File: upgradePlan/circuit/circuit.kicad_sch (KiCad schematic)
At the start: 24 parts, among them J1 Connector_GY_521, M1 Motor_DC, M2 Motor_Servo, Q1 BD249, Q2 BD249, SW1 SW_DIP_x01, U1 Freenove-SP32-WROVER, U2 L293D, U3 LM317_TO-220, U5 LM317_TO-220

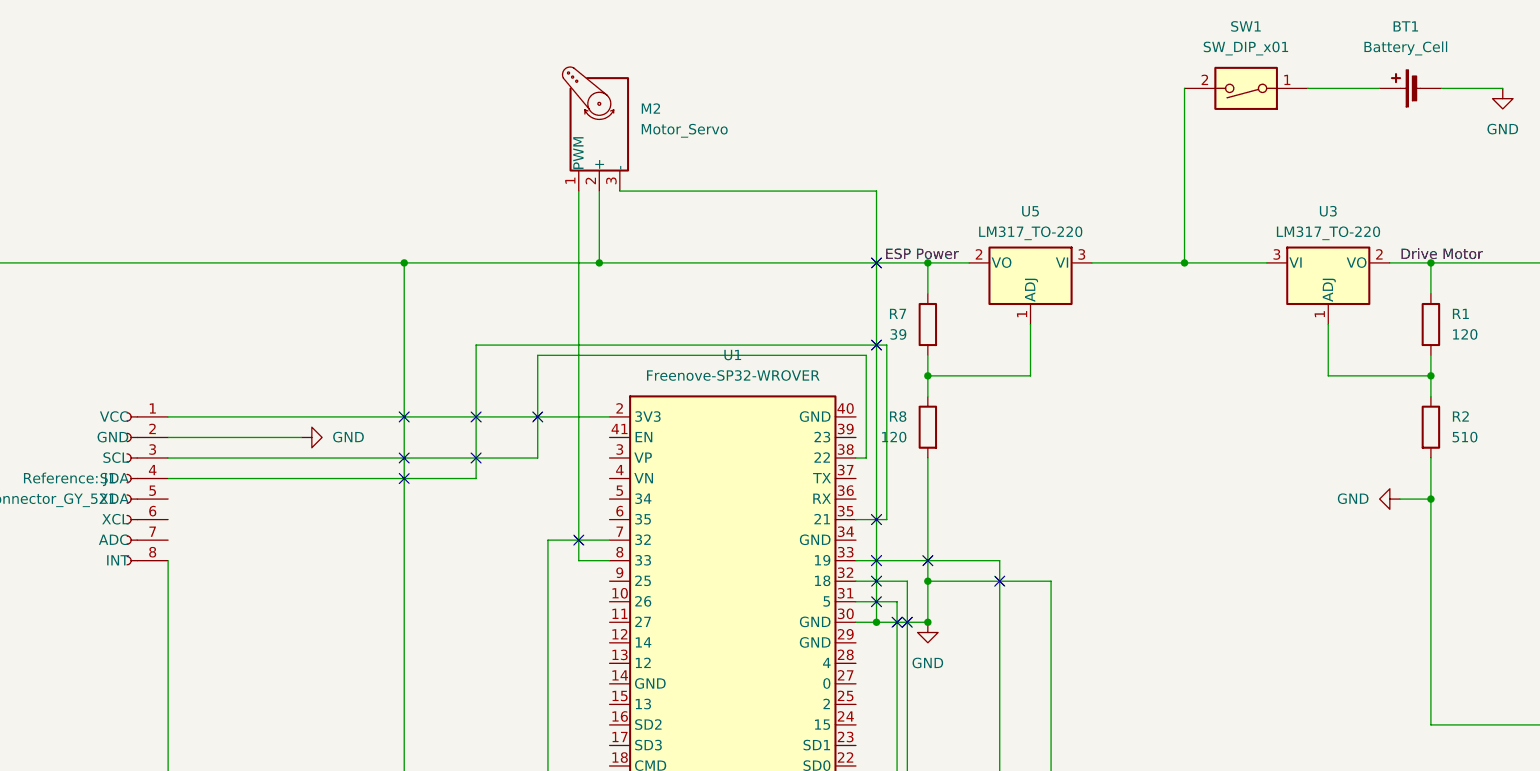
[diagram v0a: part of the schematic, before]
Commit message: Added the HC_SR04 and the tof sensor to the schematic added the recommended changes Update the read me add datasheet for hc-sr04
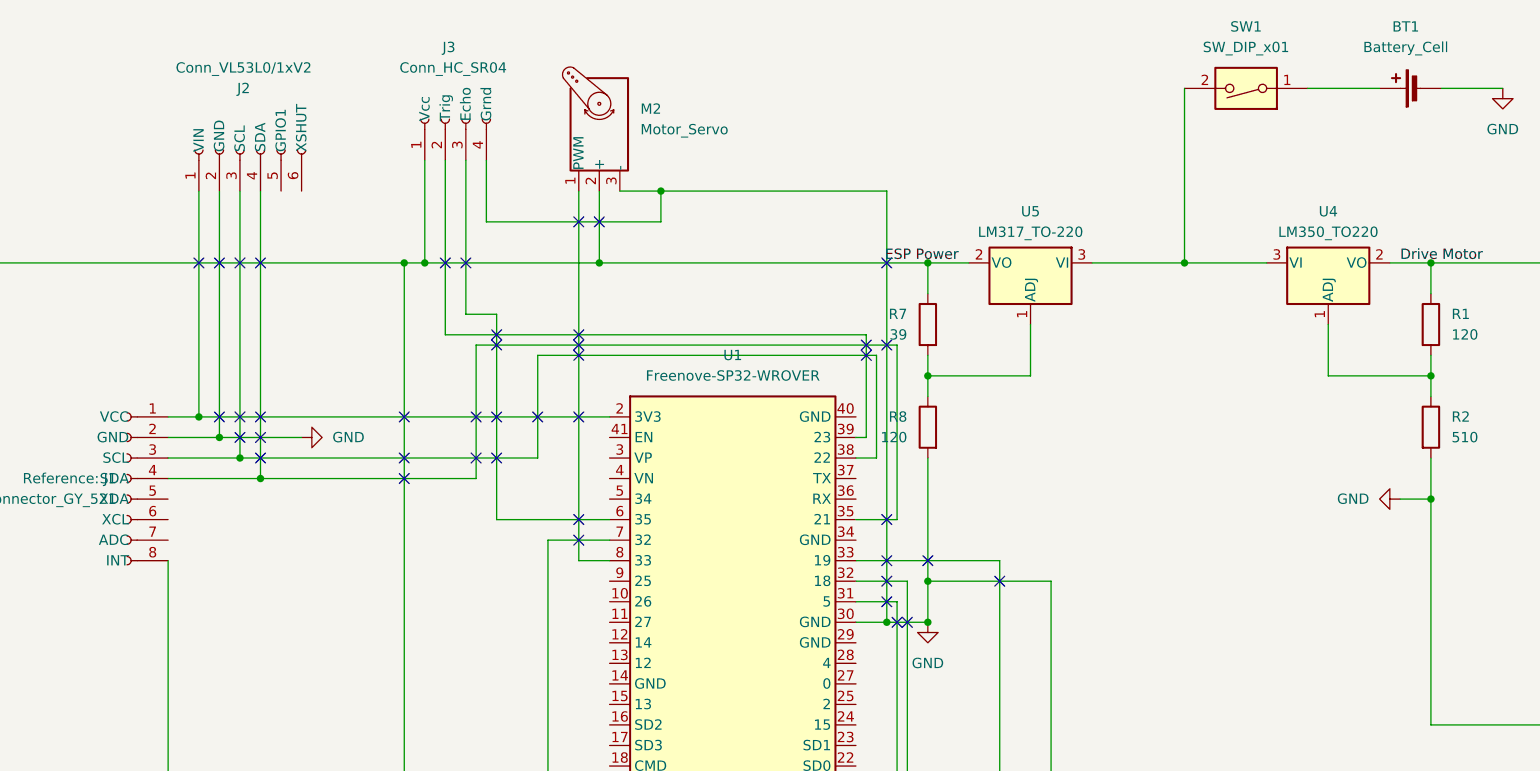
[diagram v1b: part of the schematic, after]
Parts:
- removed U3: LM317_TO-220, Package_TO_SOT_THT:TO-220-3_Vertical, symbol Regulator_Linear:LM317_TO-220
- added J2: Conn_VL53L0/1xV2, symbol Connector:Conn_01x06_Socket
- added J3: Conn_HC_SR04, symbol Connector:Conn_01x04_Socket
- added U4: LM350_TO220, Package_TO_SOT_THT:TO-220-3_Vertical, symbol Regulator_Linear:LM350_TO220
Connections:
- net Drive Motor: now also U4.2 (VO)
- net ESP Power: now also J3.1 (Vcc)
- net GND: now also J2.2 (GND), J3.4 (Grnd)
- net at SW1.2, U5.3 (VI): now also U4.3 (VI)
- net at R1.2, R2.1: now also U4.1 (ADJ)
- net at J1.1 (VCC), U1.2 (3V3): now also J2.1 (VIN)
- net at J1.3 (SCL), U1.38 (22): now also J2.3 (SCL)
- net at J1.4 (SDA), U1.35 (21): now also J2.4 (SDA)
- net at U1.39 (23): now also J3.2 (Trig)
- net at U1.6 (35): now also J3.3 (Echo)
- no-connect marks 30 -> 55

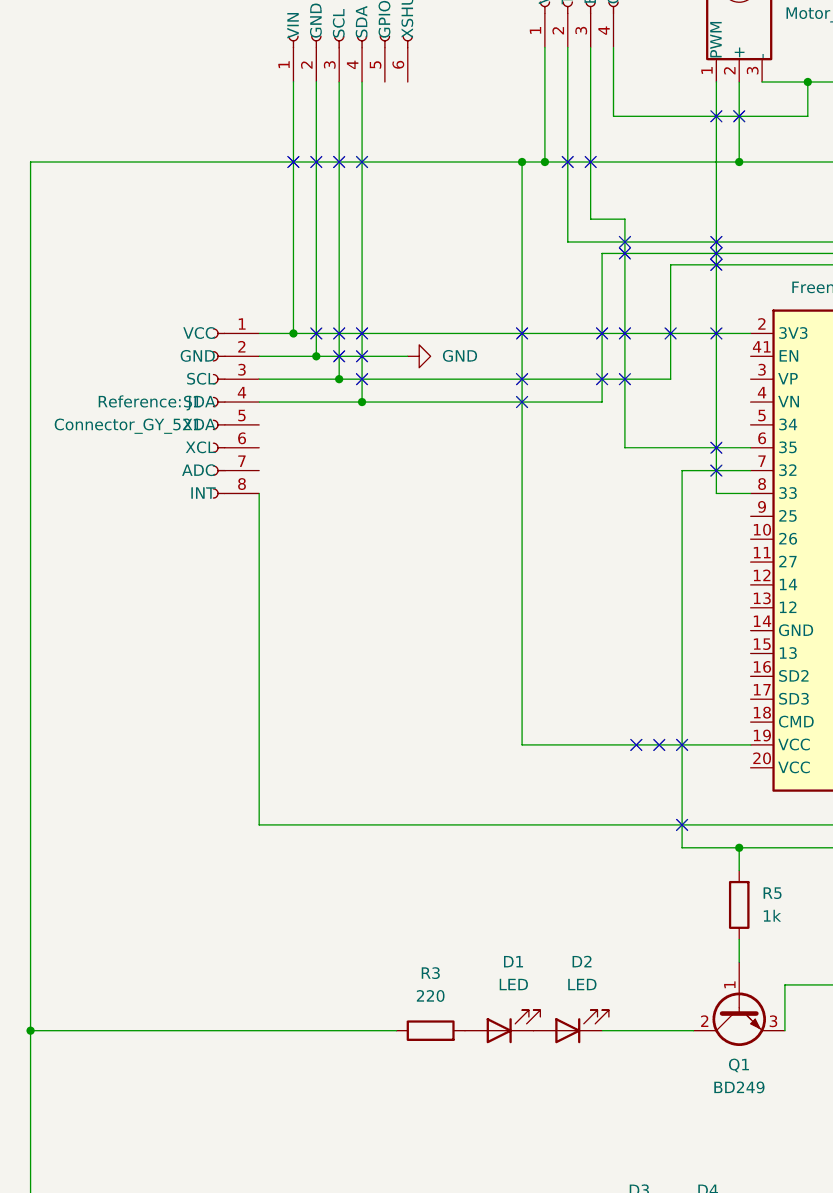
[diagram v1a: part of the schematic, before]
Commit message: Added resistor to I2C bus added setup and reading for ultrasound and tof sensor increased the max number of pub ERROR in Timer creation of the UltraSoundSensor when all others are initilized
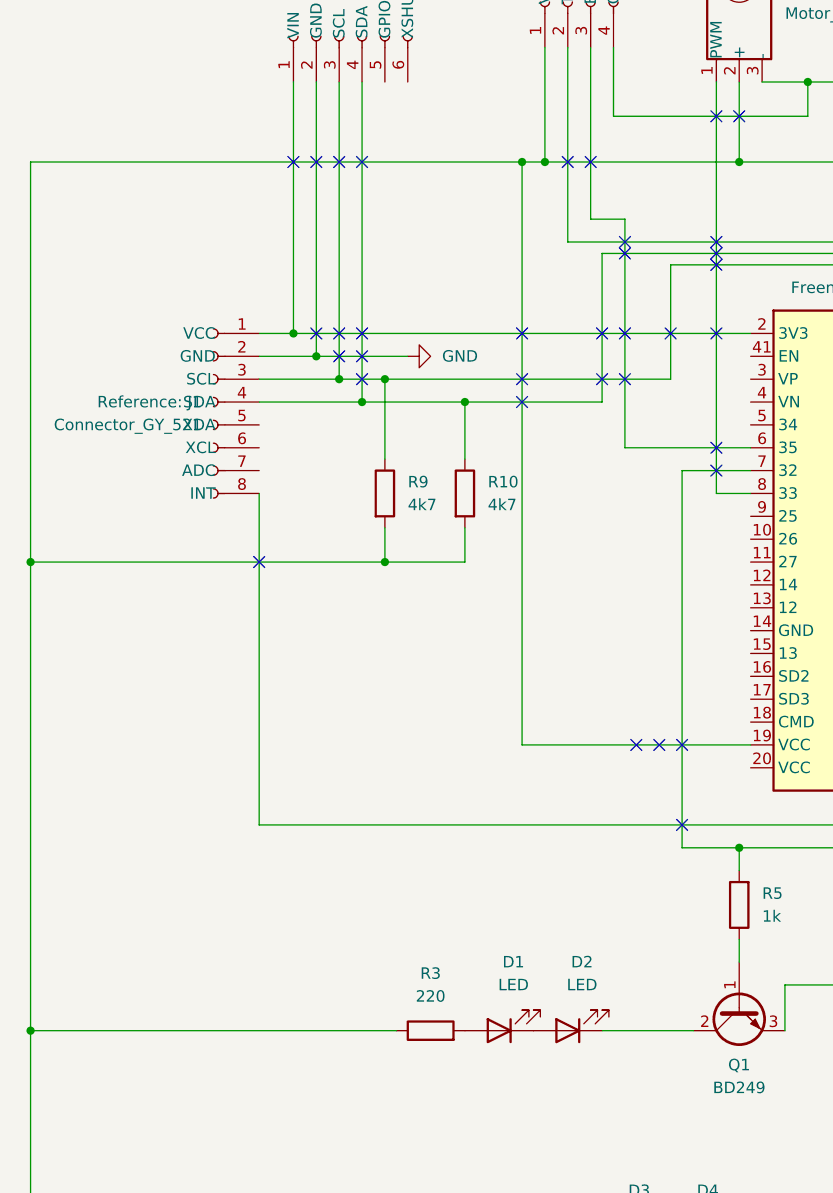
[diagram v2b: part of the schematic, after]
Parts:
- added R10, R9: 4k7, symbol Device:R
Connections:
- net ESP Power: now also R10.2, R9.2
- net at J1.3 (SCL), J2.3 (SCL), U1.38 (22): now also R9.1
- net at J1.4 (SDA), J2.4 (SDA), U1.35 (21): now also R10.1
- no-connect marks 55 -> 56
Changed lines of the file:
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@@
   (junction (at 200.66 76.2) (diameter 0) (color 0 0 0 0)
   )
+  (junction (at 67.31 73.66) (diameter 0) (color 0 0 0 0)
+  )
   (junction (at 138.43 46.99) (diameter 0) (color 0 0 0 0)
   )
@@
   (junction (at 153.67 138.43) (diameter 0) (color 0 0 0 0)
   )
+  (junction (at 58.42 91.44) (diameter 0) (color 0 0 0 0)
+  )
+  (junction (at 19.05 91.44) (diameter 0) (color 0 0 0 0)
+  )
   (junction (at 97.79 123.19) (diameter 0) (color 0 0 0 0)
   )
@@
   )
   (junction (at 48.26 66.04) (diameter 0) (color 0 0 0 0)
+  )
+  (junction (at 58.42 71.12) (diameter 0) (color 0 0 0 0)
   )
   (junction (at 266.7 72.39) (diameter 0) (color 0 0 0 0)
@@
   (no_connect (at 133.35 46.99))
   (no_connect (at 90.17 66.04))
+  (no_connect (at 44.45 91.44))
   (no_connect (at 91.44 111.76))
   (no_connect (at 53.34 68.58))
@@
     (stroke (width 0) (type default))
   )
+  (wire (pts (xy 67.31 87.63) (xy 67.31 91.44))
+    (stroke (width 0) (type default))
+  )
   (wire (pts (xy 97.79 38.1) (xy 97.79 46.99))
     (stroke (width 0) (type default))
   )
-  (wire (pts (xy 53.34 71.12) (xy 90.17 71.12))
+  (wire (pts (xy 53.34 71.12) (xy 58.42 71.12))
     (stroke (width 0) (type default))
   )
@@
     (stroke (width 0) (type default))
   )
+  (wire (pts (xy 67.31 73.66) (xy 67.31 80.01))
+    (stroke (width 0) (type default))
+  )
   (wire (pts (xy 262.89 68.58) (xy 262.89 72.39))
     (stroke (width 0) (type default))
@@
     (stroke (width 0) (type default))
   )
+  (wire (pts (xy 67.31 91.44) (xy 58.42 91.44))
+    (stroke (width 0) (type default))
+  )
   (wire (pts (xy 222.25 63.5) (xy 231.14 63.5))
     (stroke (width 0) (type default))
@@
     (stroke (width 0) (type default))
   )
+  (wire (pts (xy 19.05 91.44) (xy 19.05 143.51))
+    (stroke (width 0) (type default))
+  )
   (wire (pts (xy 151.13 54.61) (xy 151.13 60.96))
     (stroke (width 0) (type default))
@@
     (stroke (width 0) (type default))
   )
-  (wire (pts (xy 19.05 46.99) (xy 19.05 143.51))
+  (wire (pts (xy 19.05 46.99) (xy 19.05 91.44))
     (stroke (width 0) (type default))
   )
@@
     (stroke (width 0) (type default))
   )
+  (wire (pts (xy 67.31 73.66) (xy 55.88 73.66))
+    (stroke (width 0) (type default))
+  )
   (wire (pts (xy 102.87 143.51) (xy 102.87 138.43))
     (stroke (width 0) (type default))
@@
     (stroke (width 0) (type default))
   )
+  (wire (pts (xy 58.42 71.12) (xy 58.42 80.01))
+    (stroke (width 0) (type default))
+  )
   (wire (pts (xy 44.45 71.12) (xy 53.34 71.12))
     (stroke (width 0) (type default))
@@
     (stroke (width 0) (type default))
   )
-  (wire (pts (xy 82.55 73.66) (xy 55.88 73.66))
+  (wire (pts (xy 82.55 73.66) (xy 67.31 73.66))
     (stroke (width 0) (type default))
   )
@@
     (stroke (width 0) (type default))
   )
+  (wire (pts (xy 19.05 91.44) (xy 58.42 91.44))
+    (stroke (width 0) (type default))
+  )
   (wire (pts (xy 95.25 38.1) (xy 95.25 83.82))
     (stroke (width 0) (type default))
@@
     (stroke (width 0) (type default))
   )
+  (wire (pts (xy 58.42 71.12) (xy 90.17 71.12))
+    (stroke (width 0) (type default))
+  )
   (wire (pts (xy 262.89 58.42) (xy 266.7 58.42))
     (stroke (width 0) (type default))
   )
   (wire (pts (xy 124.46 129.54) (xy 124.46 125.73))
+    (stroke (width 0) (type default))
+  )
+  (wire (pts (xy 58.42 91.44) (xy 58.42 87.63))
     (stroke (width 0) (type default))
   )
@@
         (path "/330fdb5e-adb2-4f5b-81bd-20c445edd3c2"
           (reference "SW1") (unit 1)
+        )
+      )
+    )
+  )
+  (symbol (lib_id "Device:R") (at 67.31 83.82 0) (unit 1)
+    (in_bom yes) (on_board yes) (dnp no) (fields_autoplaced)
+    (property "Reference" "R10" (at 69.85 82.55 0)
+      (effects (font (size 1.27 1.27)) (justify left))
+    )
+    (property "Value" "4k7" (at 69.85 85.09 0)
+      (effects (font (size 1.27 1.27)) (justify left))
+    )
+    (property "Footprint" "" (at 65.532 83.82 90)
+      (effects (font (size 1.27 1.27)) hide)
+    )
+    (property "Datasheet" "~" (at 67.31 83.82 0)
+      (effects (font (size 1.27 1.27)) hide)
+    )
+    (pin "1")
+    (pin "2")
+    (instances
+      (project "circuit"
+        (path "/330fdb5e-adb2-4f5b-81bd-20c445edd3c2"
+          (reference "R10") (unit 1)
         )
       )
@@
         )
       )
+    )
+  )
+  (symbol (lib_id "Device:R") (at 58.42 83.82 0) (unit 1)
+    (in_bom yes) (on_board yes) (dnp no) (fields_autoplaced)
+    (property "Reference" "R9" (at 60.96 82.55 0)
+      (effects (font (size 1.27 1.27)) (justify left))
+    )
+    (property "Value" "4k7" (at 60.96 85.09 0)
+      (effects (font (size 1.27 1.27)) (justify left))
+    )
+    (property "Footprint" "" (at 56.642 83.82 90)
+      (effects (font (size 1.27 1.27)) hide)
+    )
+    (property "Datasheet" "~" (at 58.42 83.82 0)
+      (effects (font (size 1.27 1.27)) hide)
+    )
+    (pin "1")
+    (pin "2")
+    (instances
+      (project "circuit"
+        (path "/330fdb5e-adb2-4f5b-81bd-20c445edd3c2"
+          (reference "R9") (unit 1)
+        )
+      )

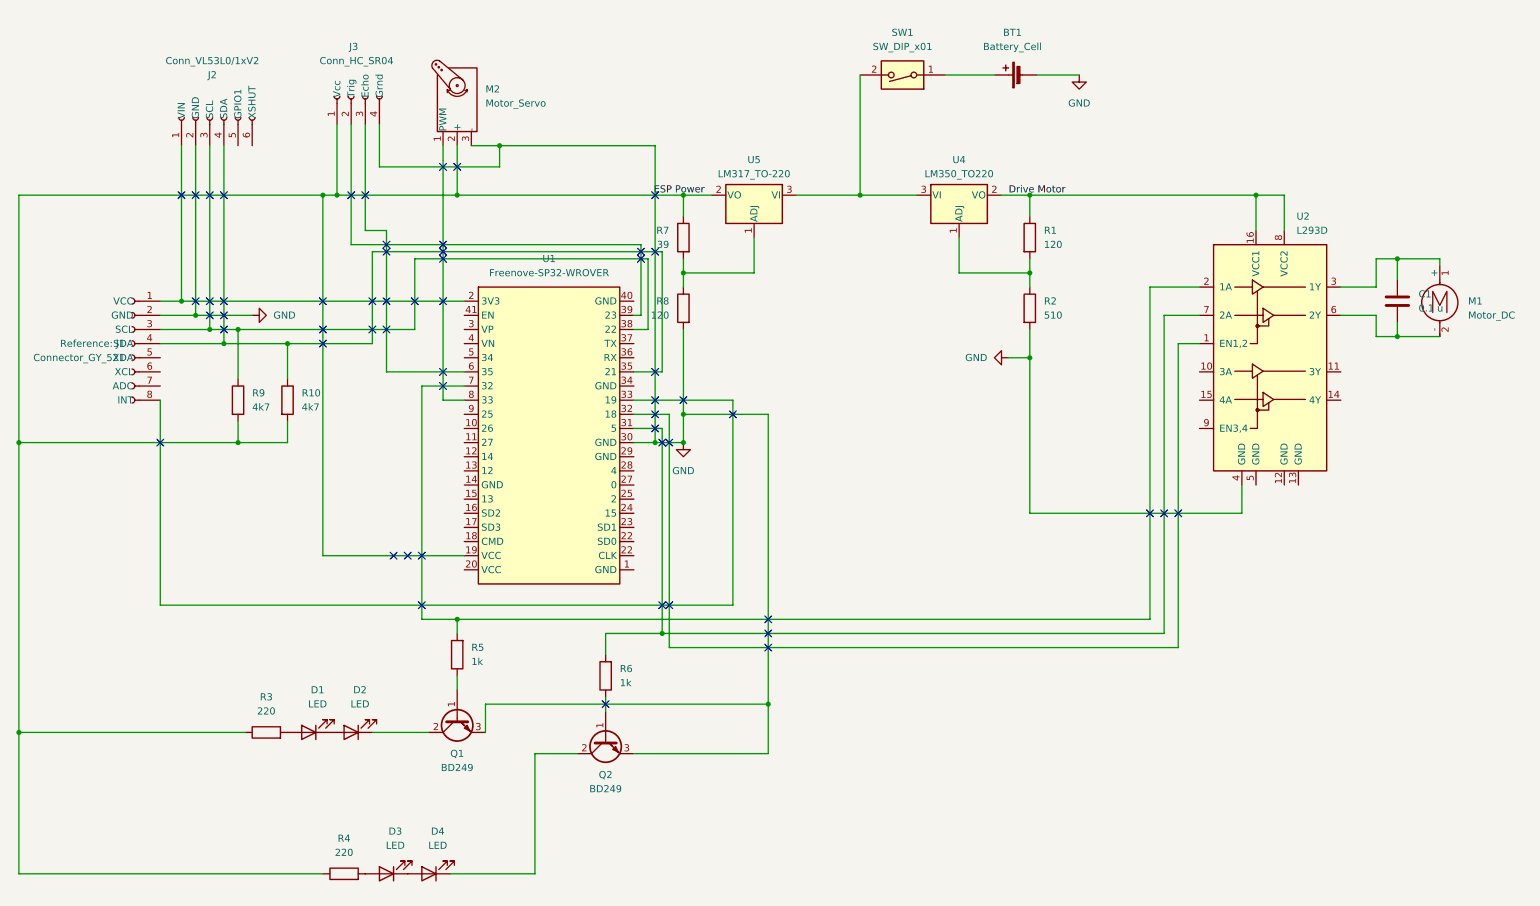
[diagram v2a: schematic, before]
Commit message: increased voltage for the motor added a signal inverter for the enable pin. Added that into the code as well
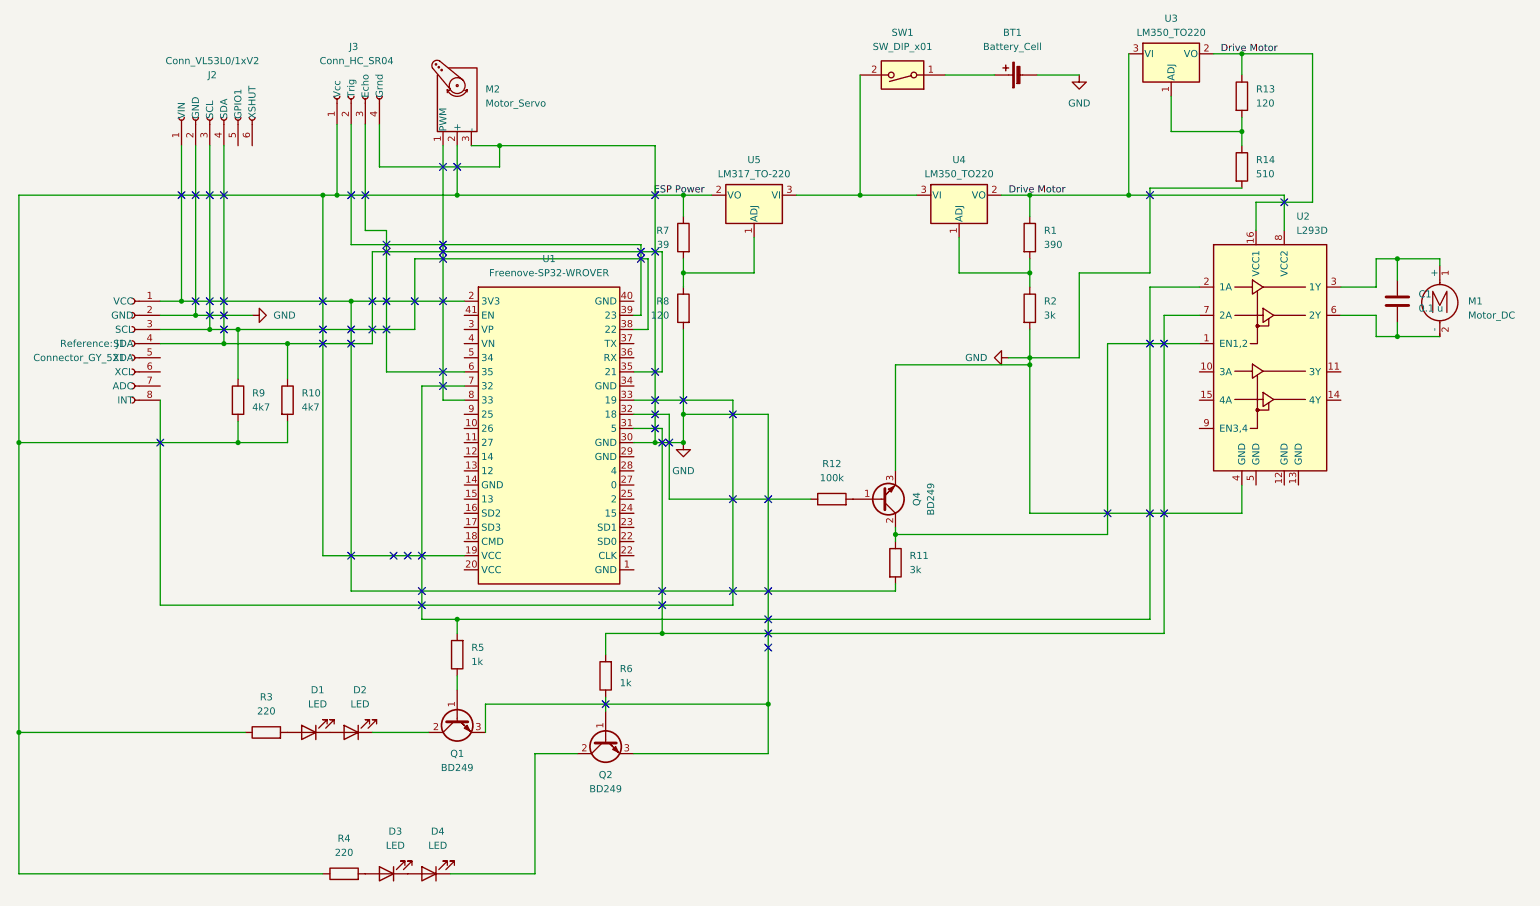
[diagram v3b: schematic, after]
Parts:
- added Q4: BD249, symbol Transistor_BJT:BD249
- added R11: 3k, symbol Device:R
- added R12: 100k, symbol Device:R
- added R13: 120, symbol Device:R
- added R14: 510, symbol Device:R
- added U3: LM350_TO220, Package_TO_SOT_THT:TO-220-3_Vertical, symbol Regulator_Linear:LM350_TO220
- R1: value 120 -> 390
- R2: value 510 -> 3k
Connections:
- net Drive Motor: now also R13.1, U3.2 (VO), U3.3 (VI)
- net GND: now also Q4.3 (E), R14.2
- net at J1.1 (VCC), J2.1 (VIN), U1.2 (3V3): now also R11.2
- net at U2.1 (EN1,2): now also Q4.2 (C), R11.1; no longer U1.32 (18)
- new net: Q4.1 (B), R12.2
- new net: R13.2, R14.1, U3.1 (ADJ)
- new net: R12.1, U1.32 (18)
- no-connect marks 56 -> 68
